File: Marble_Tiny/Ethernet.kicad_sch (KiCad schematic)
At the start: 38 parts, among them J3 BELFUSE_0826-1G1T-43-F, Q1 XTAL_25MHZ_EPSON_TSX-3225_25.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, U7 RTL8211F-CG

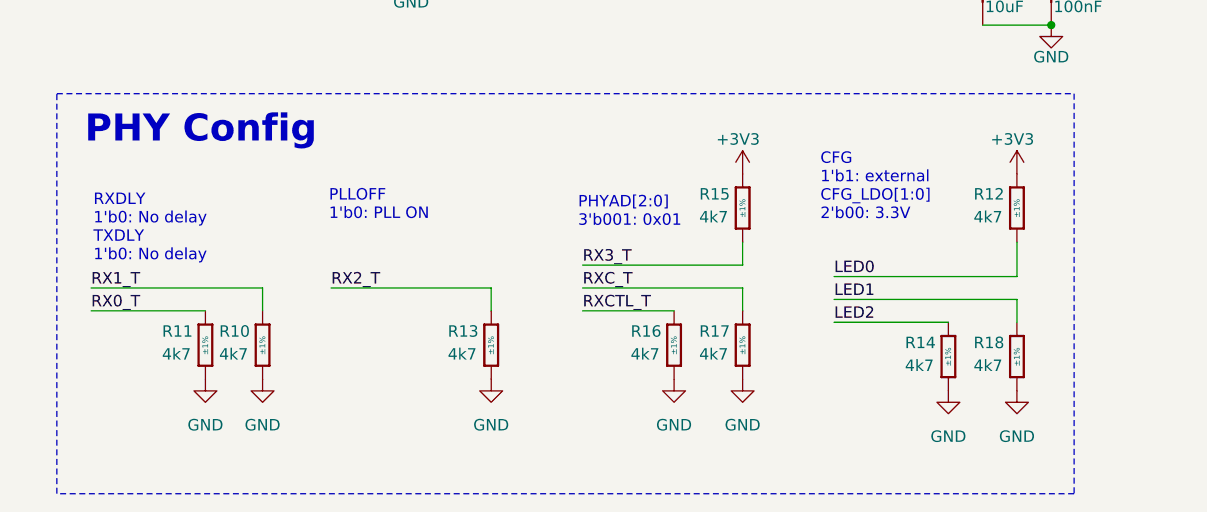
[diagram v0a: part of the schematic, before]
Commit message: components placement done, fixed issue with PCB
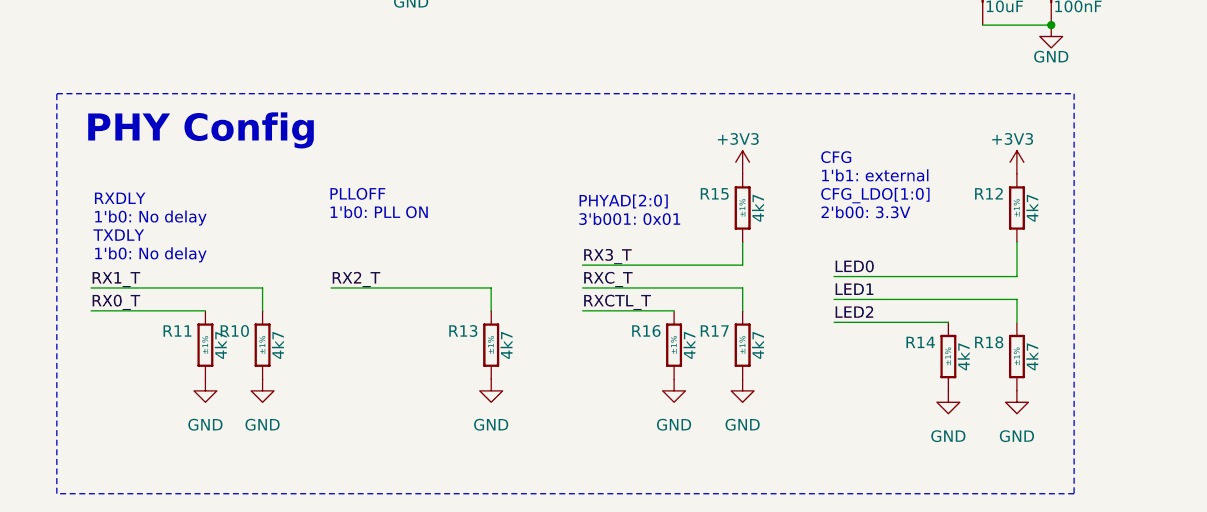
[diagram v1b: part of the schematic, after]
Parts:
- R10, R11, R12, R13, R14, R15, R16, R17, R18: value R1210_4K7_1%_0.5W_100PPM -> R0402_4K7_1%_0.0625W_100PPM; footprint Resistors SMD:RESC3225X70N -> Resistors SMD:RESC1005X40N; symbol Resistors SMD:R1210_4K7_1%_0.5W_100PPM -> Resistors SMD:R0402_4K7_1%_0.0625W_100PPM; Author CERN DEM WB -> CERN DEM JLC; Case 1210 -> 0402; ComponentHeight 0.7mm -> (none); CreateDate 06/30/21 00:00:00 -> 12/03/07 00:00:00; Footprint Ref RESC3225X70N -> RESC1005X40N; HelpURL \\cern.ch\dfs\Applications\Altium\Datasheets\R1210_VISHAY_C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 -> \\cern.ch\dfs\Applications\Altium\Datasheets\R0402_Phycomp_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; LatestRevisionDate 06/30/21 00:00:00 -> 10/17/12 00:00:00; Manufacturer Part Number R1210_4K7_1%_0.5W_100PPM -> R0402_4K7_1%_0.0625W_100PPM; Manufacturer1 ComponentHeight 0.7mm -> 0.4mm; Manufacturer1 Example VISHAY -> YAGEO PHYCOMP; Manufacturer1 Part Number CRCW12104K70FK -> 232270674702L; Part Number R1210_4K7_1%_0.5W_100PPM -> R0402_4K7_1%_0.0625W_100PPM; Power 0.5W -> 0.0625W; Status None -> Not Recommended
